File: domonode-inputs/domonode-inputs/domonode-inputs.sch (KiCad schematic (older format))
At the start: 65 parts, among them P1 CONN_01X02, P10 CONN_01X02, P11 CONN_01X02, P12 CONN_02X03, P13 CONN_02X05, P14 CONN_01X06, P2 CONN_01X02, P3 CONN_01X02, P4 CONN_01X02, P5 CONN_01X02, P6 CONN_01X02, P7 CONN_01X02, P8 CONN_01X02, P9 CONN_01X02, U1 TLP620, U10 TLP620, U11 PCA9555, U12 24LC02, U13 TLP620, U2 TLP620, U3 TLP620, U4 TLP620, U5 TLP620, U6 TLP620, U7 TLP620, U8 TLP620, U9 TLP620

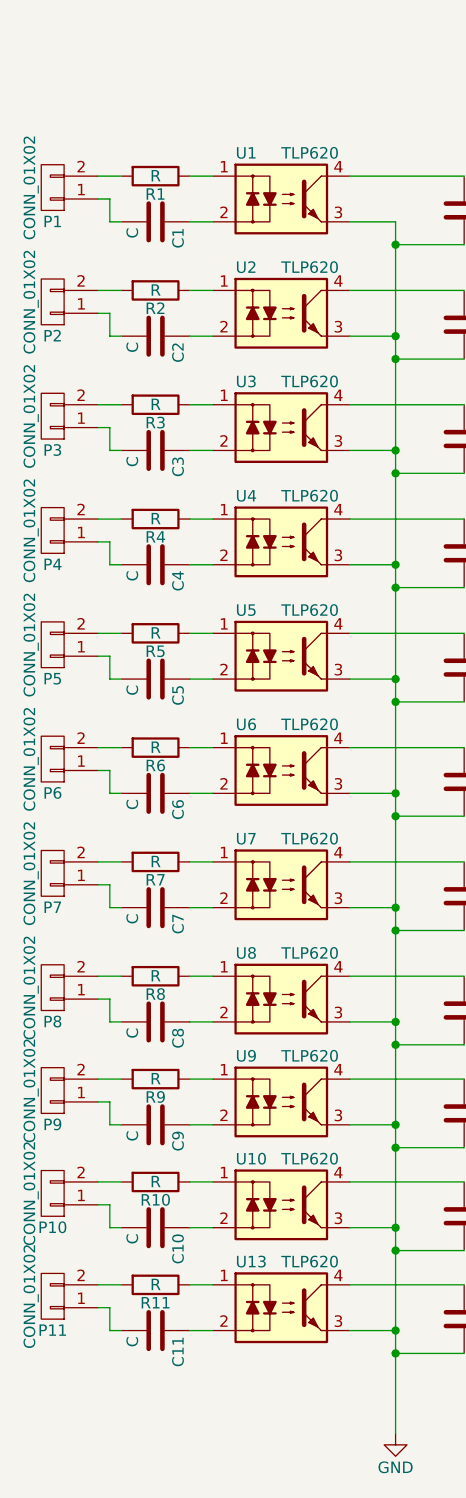
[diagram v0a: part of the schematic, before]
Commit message: Reorganized DomoNode-Inputs files and added gerbers
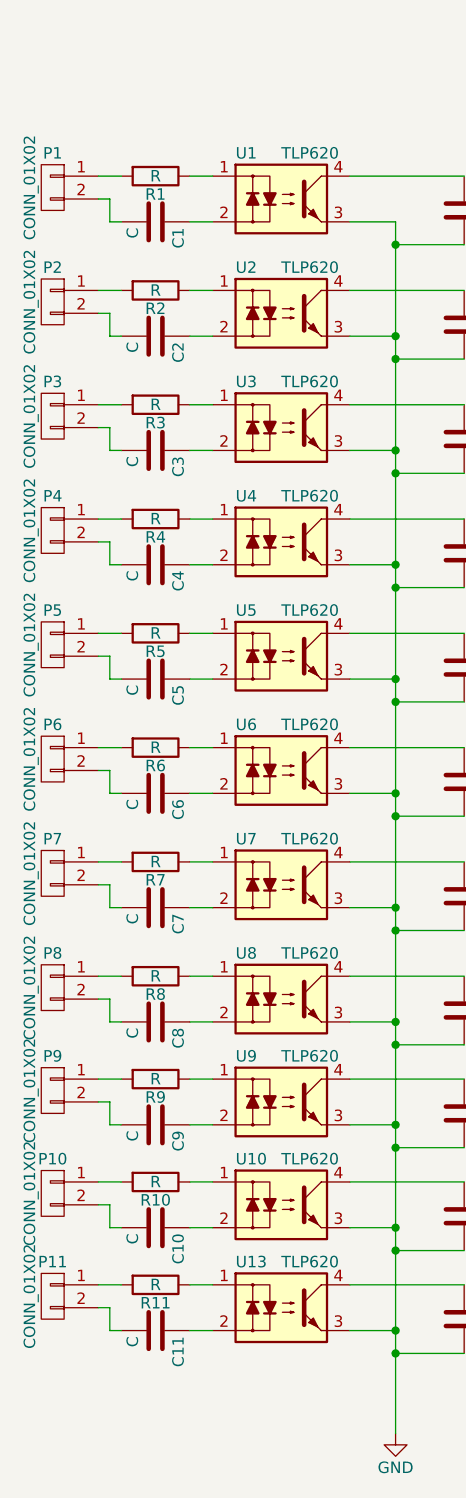
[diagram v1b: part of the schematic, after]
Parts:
- P1, P10, P11, P2, P3, P4, P5, P6, P7, P8, P9: footprint AAA mie lib verificate:ScrewTerm_2x3.81 -> AAA mie lib verificate:KF2EDGK-5.08-2
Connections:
- net at P1.1 (P1): now also R1.2; no longer C1.2
- net at P1.2 (P2): now also C1.2; no longer R1.2
- net at P2.1 (P1): now also R2.2; no longer C2.2
- net at P2.2 (P2): now also C2.2; no longer R2.2
- net at P3.1 (P1): now also R3.2; no longer C3.2
- net at P3.2 (P2): now also C3.2; no longer R3.2
- net at P4.1 (P1): now also R4.2; no longer C4.2
- net at P4.2 (P2): now also C4.2; no longer R4.2
- net at P5.1 (P1): now also R5.2; no longer C5.2
- net at P5.2 (P2): now also C5.2; no longer R5.2
- net at P6.1 (P1): now also R6.2; no longer C6.2
- net at P6.2 (P2): now also C6.2; no longer R6.2
- net at P7.1 (P1): now also R7.2; no longer C7.2
- net at P7.2 (P2): now also C7.2; no longer R7.2
- net at P8.1 (P1): now also R8.2; no longer C8.2
- net at P8.2 (P2): now also C8.2; no longer R8.2
- net at P9.1 (P1): now also R9.2; no longer C9.2
- net at P9.2 (P2): now also C9.2; no longer R9.2
- net at P10.1 (P1): now also R10.2; no longer C10.2
- net at P10.2 (P2): now also C10.2; no longer R10.2
- net at P11.1 (P1): now also R11.2; no longer C11.2
- net at P11.2 (P2): now also C11.2; no longer R11.2
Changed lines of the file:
@@
 F 0 "P1" H 1650 1750 50  0000 C CNN
 F 1 "CONN_01X02" V 1750 1600 50  0000 C CNN
-F 2 "AAA mie lib verificate:ScrewTerm_2x3.81" H 1650 1600 50  0001 C CNN
+F 2 "AAA mie lib verificate:KF2EDGK-5.08-2" H 1650 1600 50  0001 C CNN
 F 3 "" H 1650 1600 50  0000 C CNN
 	1    1650 1600
-	-1   0    0    1
+	-1   0    0    -1
 $EndComp
 $Comp
@@
 F 0 "P2" H 1650 2250 50  0000 C CNN
 F 1 "CONN_01X02" V 1750 2100 50  0000 C CNN
-F 2 "AAA mie lib verificate:ScrewTerm_2x3.81" H 1650 2100 50  0001 C CNN
+F 2 "AAA mie lib verificate:KF2EDGK-5.08-2" H 1650 2100 50  0001 C CNN
 F 3 "" H 1650 2100 50  0000 C CNN
 	1    1650 2100
-	-1   0    0    1
+	-1   0    0    -1
 $EndComp
 $Comp
@@
 F 0 "P3" H 1650 2750 50  0000 C CNN
 F 1 "CONN_01X02" V 1750 2600 50  0000 C CNN
-F 2 "AAA mie lib verificate:ScrewTerm_2x3.81" H 1650 2600 50  0001 C CNN
+F 2 "AAA mie lib verificate:KF2EDGK-5.08-2" H 1650 2600 50  0001 C CNN
 F 3 "" H 1650 2600 50  0000 C CNN
 	1    1650 2600
-	-1   0    0    1
+	-1   0    0    -1
 $EndComp
 $Comp
@@
 F 0 "P4" H 1650 3250 50  0000 C CNN
 F 1 "CONN_01X02" V 1750 3100 50  0000 C CNN
-F 2 "AAA mie lib verificate:ScrewTerm_2x3.81" H 1650 3100 50  0001 C CNN
+F 2 "AAA mie lib verificate:KF2EDGK-5.08-2" H 1650 3100 50  0001 C CNN
 F 3 "" H 1650 3100 50  0000 C CNN
 	1    1650 3100
-	-1   0    0    1
+	-1   0    0    -1
 $EndComp
 $Comp
@@
 F 0 "P5" H 1650 3750 50  0000 C CNN
 F 1 "CONN_01X02" V 1750 3600 50  0000 C CNN
-F 2 "AAA mie lib verificate:ScrewTerm_2x3.81" H 1650 3600 50  0001 C CNN
+F 2 "AAA mie lib verificate:KF2EDGK-5.08-2" H 1650 3600 50  0001 C CNN
 F 3 "" H 1650 3600 50  0000 C CNN
 	1    1650 3600
-	-1   0    0    1
+	-1   0    0    -1
 $EndComp
 $Comp
@@
 F 0 "P6" H 1650 4250 50  0000 C CNN
 F 1 "CONN_01X02" V 1750 4100 50  0000 C CNN
-F 2 "AAA mie lib verificate:ScrewTerm_2x3.81" H 1650 4100 50  0001 C CNN
+F 2 "AAA mie lib verificate:KF2EDGK-5.08-2" H 1650 4100 50  0001 C CNN
 F 3 "" H 1650 4100 50  0000 C CNN
 	1    1650 4100
-	-1   0    0    1
+	-1   0    0    -1
 $EndComp
 $Comp
@@
 F 0 "P7" H 1650 4750 50  0000 C CNN
 F 1 "CONN_01X02" V 1750 4600 50  0000 C CNN
-F 2 "AAA mie lib verificate:ScrewTerm_2x3.81" H 1650 4600 50  0001 C CNN
+F 2 "AAA mie lib verificate:KF2EDGK-5.08-2" H 1650 4600 50  0001 C CNN
 F 3 "" H 1650 4600 50  0000 C CNN
 	1    1650 4600
-	-1   0    0    1
+	-1   0    0    -1
 $EndComp
 $Comp
@@
 F 0 "P8" H 1650 5250 50  0000 C CNN
 F 1 "CONN_01X02" V 1750 5100 50  0000 C CNN
-F 2 "AAA mie lib verificate:ScrewTerm_2x3.81" H 1650 5100 50  0001 C CNN
+F 2 "AAA mie lib verificate:KF2EDGK-5.08-2" H 1650 5100 50  0001 C CNN
 F 3 "" H 1650 5100 50  0000 C CNN
 	1    1650 5100
-	-1   0    0    1
+	-1   0    0    -1
 $EndComp
 $Comp
@@
 F 0 "P9" H 1650 5700 50  0000 C CNN
 F 1 "CONN_01X02" V 1750 5550 50  0000 C CNN
-F 2 "AAA mie lib verificate:ScrewTerm_2x3.81" H 1650 5550 50  0001 C CNN
+F 2 "AAA mie lib verificate:KF2EDGK-5.08-2" H 1650 5550 50  0001 C CNN
 F 3 "" H 1650 5550 50  0000 C CNN
 	1    1650 5550
-	-1   0    0    1
+	-1   0    0    -1
 $EndComp
 $Comp
@@
 F 0 "P10" H 1650 6150 50  0000 C CNN
 F 1 "CONN_01X02" V 1750 6000 50  0000 C CNN
-F 2 "AAA mie lib verificate:ScrewTerm_2x3.81" H 1650 6000 50  0001 C CNN
+F 2 "AAA mie lib verificate:KF2EDGK-5.08-2" H 1650 6000 50  0001 C CNN
 F 3 "" H 1650 6000 50  0000 C CNN
 	1    1650 6000
-	-1   0    0    1
+	-1   0    0    -1
 $EndComp
 $Comp
@@
 F 0 "P11" H 1650 6600 50  0000 C CNN
 F 1 "CONN_01X02" V 1750 6450 50  0000 C CNN
-F 2 "AAA mie lib verificate:ScrewTerm_2x3.81" H 1650 6450 50  0001 C CNN
+F 2 "AAA mie lib verificate:KF2EDGK-5.08-2" H 1650 6450 50  0001 C CNN
 F 3 "" H 1650 6450 50  0000 C CNN
 	1    1650 6450
-	-1   0    0    1
-$EndComp
-$Comp
+	-1   0    0    -1
+$EndComp
+$Comp

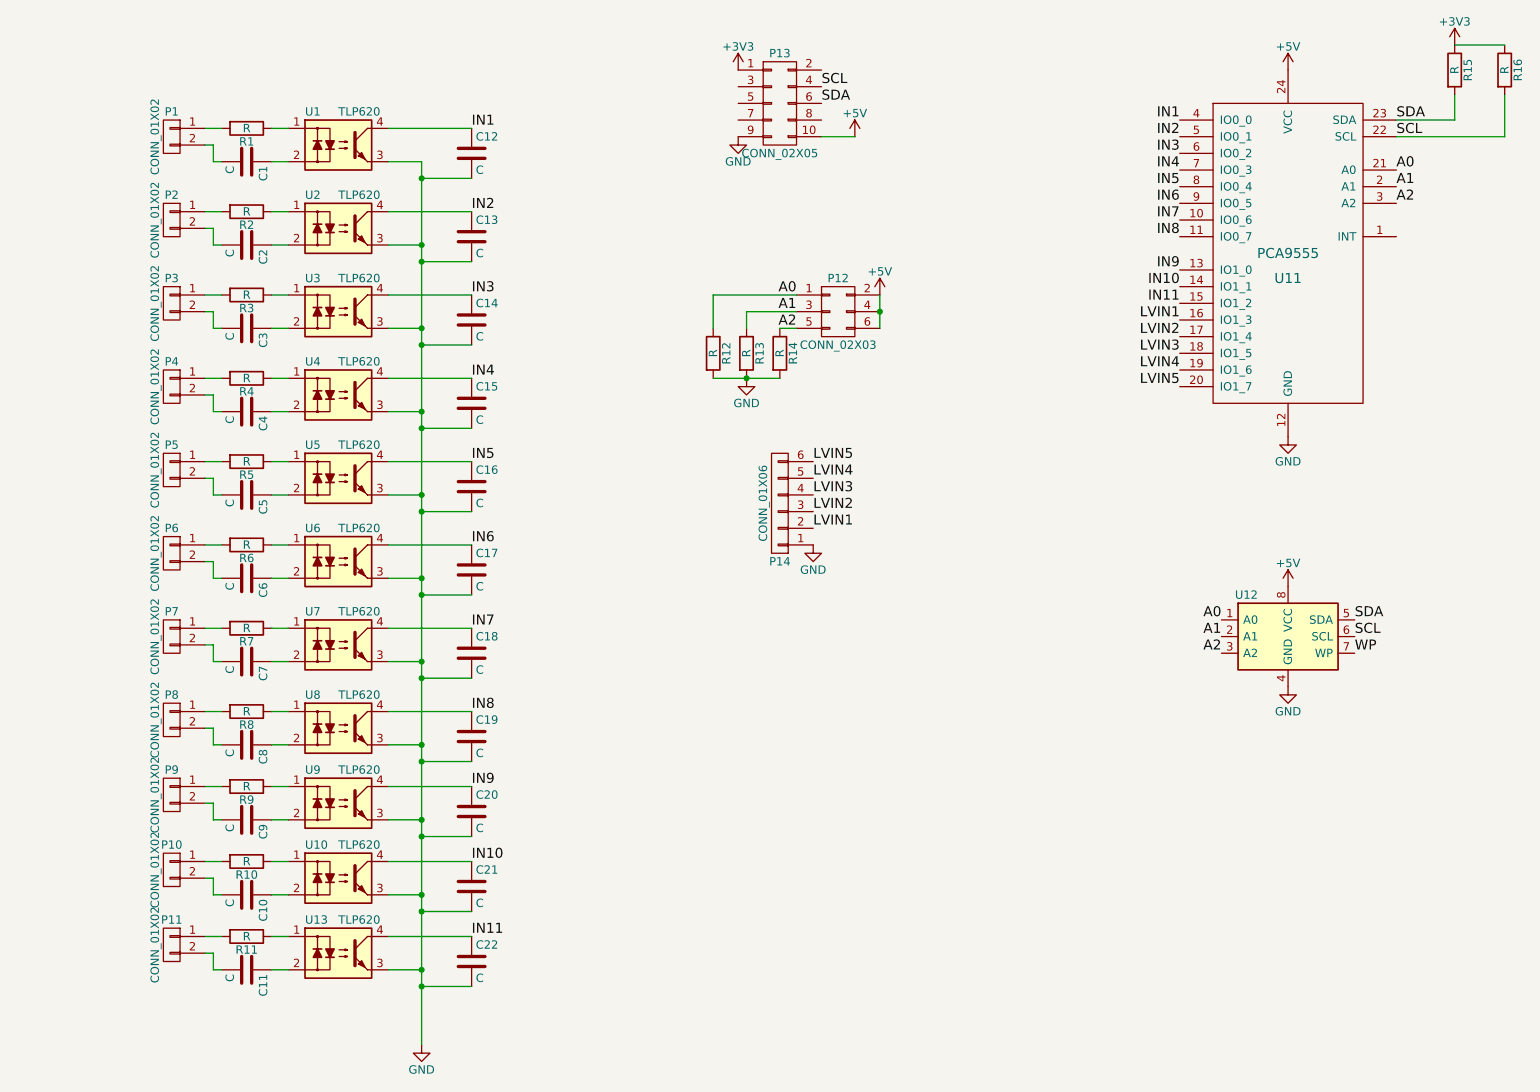
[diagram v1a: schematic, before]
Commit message: Updated DomoNode-Inputs design files: - added component values in schematic (w/ minor changes for readability) - changed X2 capacitors footprint - moved filter capacitors to a regular pattern, where possible - slightly changed layout to account for new footprints
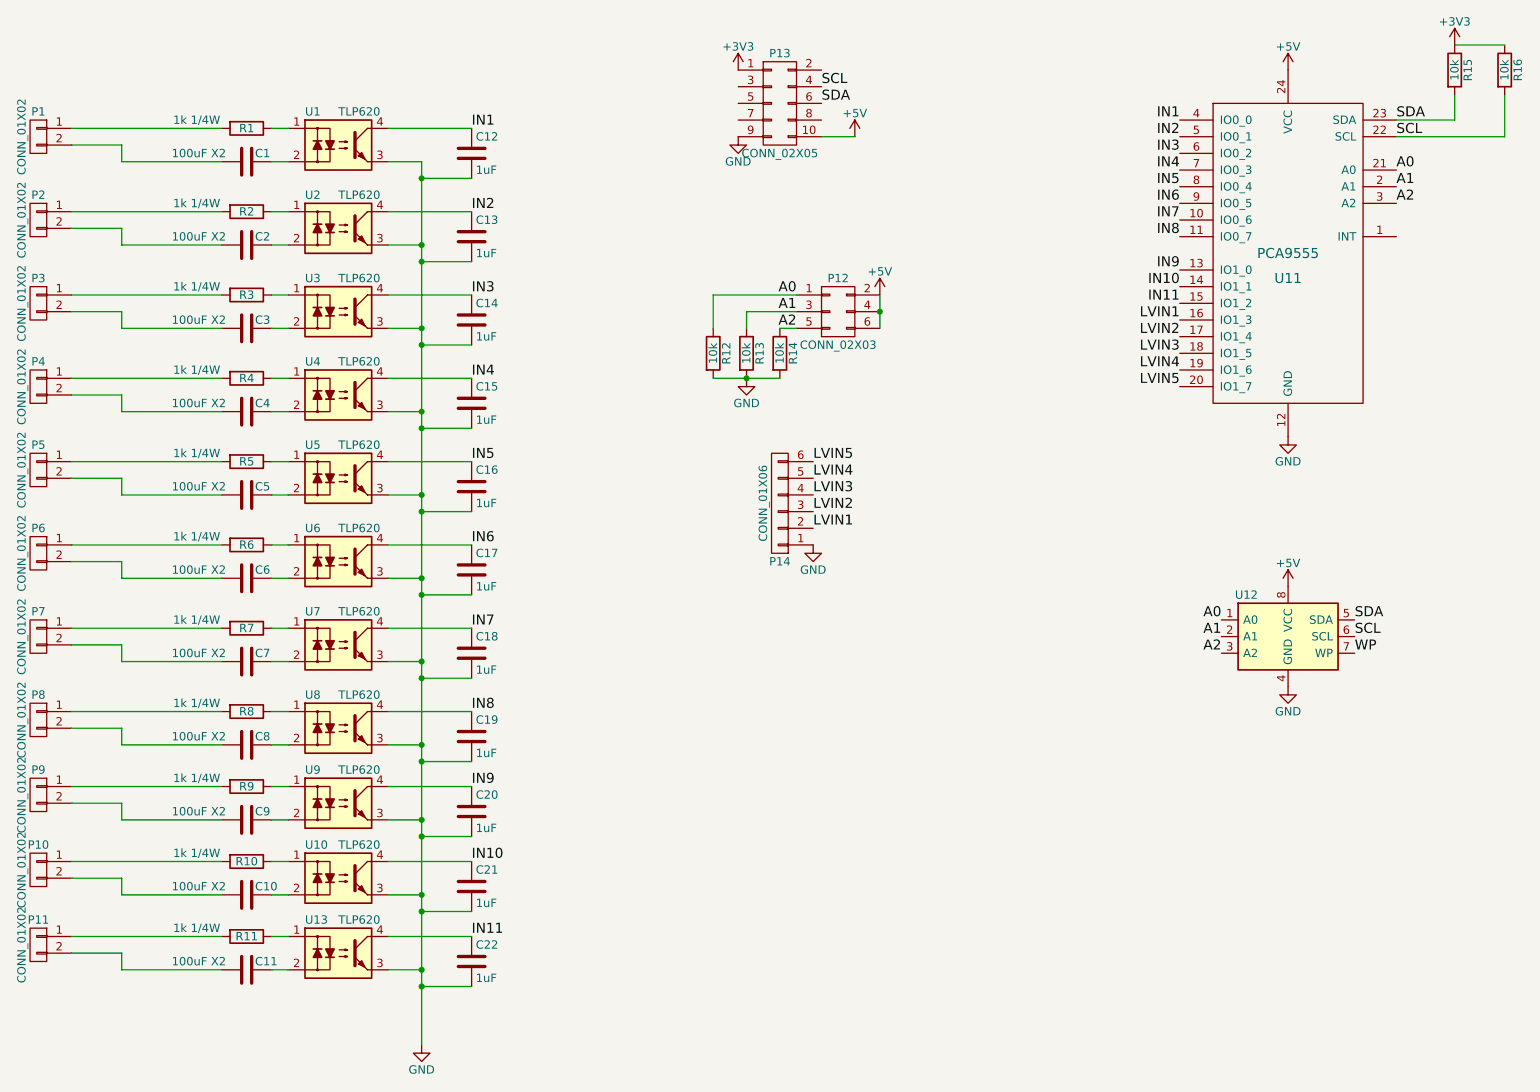
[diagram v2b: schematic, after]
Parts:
- C1, C10, C11, C2, C3, C4, C5, C6, C7, C8, C9: value C -> 100uF X2; footprint Capacitors_ThroughHole:C_Rect_L18.0mm_W6.0mm_P15.00mm_FKS3_FKP3 -> Capacitors_ThroughHole:C_Rect_L13.0mm_W6.0mm_P10.00mm_FKS3_FKP3_MKS4
- C12, C13, C14, C15, C16, C17, C18, C19, C20, C21, C22: value C -> 1uF
- R1, R10, R11, R2, R3, R4, R5, R6, R7, R8, R9: value R -> 1k 1/4W
- R12, R13, R14, R15, R16: value R -> 10k
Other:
- moved on the sheet: P1, P10, P11, P2, P3, P4, P5, P6, P7, P8, P9
